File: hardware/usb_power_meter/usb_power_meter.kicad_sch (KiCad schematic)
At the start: 21 parts, among them U1 nRF52833-QDxx, X1 32.768kHz crystal, X2 32Mhz crystal

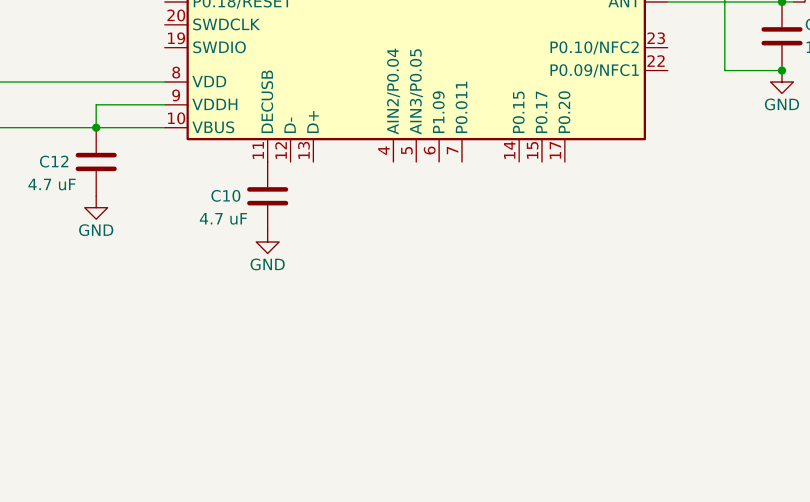
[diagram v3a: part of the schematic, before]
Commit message: Add INA226
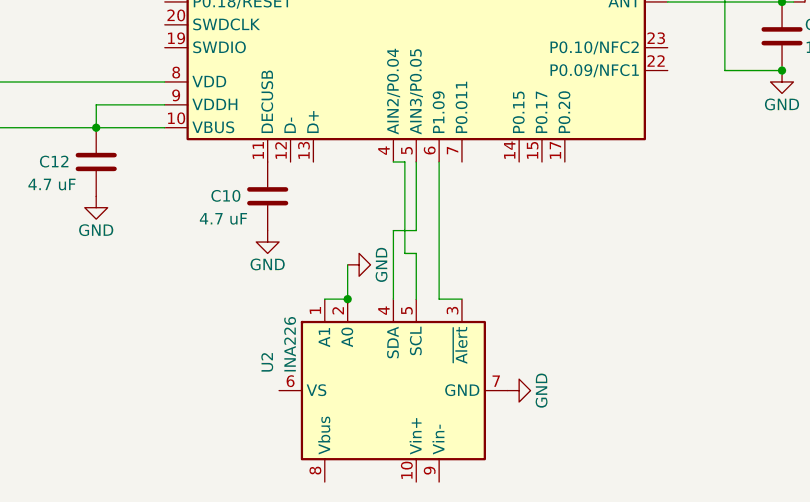
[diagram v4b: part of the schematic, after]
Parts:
- added U2: INA226, Package_SO:VSSOP-10_3x3mm_P0.5mm, symbol Ostranna:INA226
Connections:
- net GND: now also U2.1 (A1), U2.2 (A0), U2.7 (GND)
- net at U1.4 (AIN2/P0.04): now also U2.5 (SCL)
- net at U1.5 (AIN3/P0.05): now also U2.4 (SDA)
- net at U1.6 (P1.09): now also U2.3 (~{Alert})
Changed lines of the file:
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@@
   (junction (at 198.12 113.03) (diameter 0) (color 0 0 0 0)
+  )
+  (junction (at 138.43 146.05) (diameter 0) (color 0 0 0 0)
   )
   (junction (at 87.63 104.14) (diameter 0) (color 0 0 0 0)
@@
     (stroke (width 0) (type default))
   )
+  (wire (pts (xy 144.78 140.97) (xy 144.78 130.81))
+    (stroke (width 0) (type default))
+  )
+  (wire (pts (xy 143.51 138.43) (xy 146.05 138.43))
+    (stroke (width 0) (type default))
+  )
   (wire (pts (xy 83.82 111.76) (xy 87.63 111.76))
     (stroke (width 0) (type default))
@@
     (stroke (width 0) (type default))
   )
+  (wire (pts (xy 146.05 146.05) (xy 146.05 140.97))
+    (stroke (width 0) (type default))
+  )
   (wire (pts (xy 148.59 62.23) (xy 152.4 62.23))
     (stroke (width 0) (type default))
@@
     (stroke (width 0) (type default))
   )
+  (wire (pts (xy 146.05 140.97) (xy 144.78 140.97))
+    (stroke (width 0) (type default))
+  )
   (wire (pts (xy 148.59 80.01) (xy 148.59 62.23))
     (stroke (width 0) (type default))
@@
     (stroke (width 0) (type default))
   )
+  (wire (pts (xy 148.59 146.05) (xy 148.59 130.81))
+    (stroke (width 0) (type default))
+  )
   (wire (pts (xy 120.65 90.17) (xy 115.57 90.17))
     (stroke (width 0) (type default))
@@
     (stroke (width 0) (type default))
   )
+  (wire (pts (xy 138.43 146.05) (xy 138.43 142.24))
+    (stroke (width 0) (type default))
+  )
   (wire (pts (xy 102.87 88.9) (xy 96.52 88.9))
     (stroke (width 0) (type default))
@@
     (stroke (width 0) (type default))
   )
+  (wire (pts (xy 146.05 138.43) (xy 146.05 130.81))
+    (stroke (width 0) (type default))
+  )
   (wire (pts (xy 133.35 62.23) (xy 135.89 62.23))
     (stroke (width 0) (type default))
@@
     (stroke (width 0) (type default))
   )
+  (wire (pts (xy 151.13 146.05) (xy 148.59 146.05))
+    (stroke (width 0) (type default))
+  )
+  (wire (pts (xy 144.78 130.81) (xy 143.51 130.81))
+    (stroke (width 0) (type default))
+  )
   (wire (pts (xy 67.31 121.92) (xy 118.11 121.92))
     (stroke (width 0) (type default))
@@
     (stroke (width 0) (type default))
   )
+  (wire (pts (xy 135.89 146.05) (xy 138.43 146.05))
+    (stroke (width 0) (type default))
+  )
   (wire (pts (xy 118.11 106.68) (xy 102.87 106.68))
     (stroke (width 0) (type default))
   )
   (wire (pts (xy 134.62 71.12) (xy 133.35 71.12))
+    (stroke (width 0) (type default))
+  )
+  (wire (pts (xy 143.51 146.05) (xy 143.51 138.43))
     (stroke (width 0) (type default))
   )
@@
     )
   )
+  (symbol (lib_id "Ostranna:INA226") (at 143.51 156.21 90) (unit 1)
+    (in_bom yes) (on_board yes) (dnp no) (fields_autoplaced)
+    (property "Reference" "U2" (at 129.54 154.2541 0)
+      (effects (font (size 1.27 1.27)) (justify left))
+    )
+    (property "Value" "INA226" (at 132.08 154.2541 0)
+      (effects (font (size 1.27 1.27)) (justify left))
+    )
+    (property "Footprint" "Package_SO:VSSOP-10_3x3mm_P0.5mm" (at 154.94 135.89 0)
+      (effects (font (size 1.27 1.27)) hide)
+    )
+    (property "Datasheet" "http://www.ti.com/lit/ds/symlink/ina226.pdf" (at 146.05 147.32 0)
+      (effects (font (size 1.27 1.27)) hide)
+    )
+    (property "LCSC" "C49851" (at 143.51 156.21 0)
+      (effects (font (size 1.27 1.27)) hide)
+    )
+    (pin "1")
+    (pin "10")
+    (pin "2")
+    (pin "3")
+    (pin "4")
+    (pin "5")
+    (pin "6")
+    (pin "7")
+    (pin "8")
+    (pin "9")
+    (instances
+      (project "usb_power_meter"
+        (path "/991df1c7-1ea4-4c32-892f-6236282859f6"
+          (reference "U2") (unit 1)
+        )
+      )
+    )
+  )
   (symbol (lib_id "power:GND") (at 86.36 97.79 0) (unit 1)
     (in_bom yes) (on_board yes) (dnp no)
@@
         (path "/991df1c7-1ea4-4c32-892f-6236282859f6"
           (reference "#PWR04") (unit 1)
+        )
+      )
+    )
+  )
+  (symbol (lib_id "power:GND") (at 156.21 156.21 90) (unit 1)
+    (in_bom yes) (on_board yes) (dnp no)
+    (property "Reference" "#PWR020" (at 162.56 156.21 0)
+      (effects (font (size 1.27 1.27)) hide)
+    )
+    (property "Value" "GND" (at 160.02 156.21 0)
+      (effects (font (size 1.27 1.27)))
+    )
+    (property "Footprint" "" (at 156.21 156.21 0)
+      (effects (font (size 1.27 1.27)) hide)
+    )
+    (property "Datasheet" "" (at 156.21 156.21 0)
+      (effects (font (size 1.27 1.27)) hide)
+    )
+    (pin "1")
+    (instances
+      (project "usb_power_meter"
+        (path "/991df1c7-1ea4-4c32-892f-6236282859f6"
+          (reference "#PWR020") (unit 1)
         )
       )
@@
         )
       )
+    )
+  )
+  (symbol (lib_id "power:GND") (at 138.43 142.24 90) (unit 1)
+    (in_bom yes) (on_board yes) (dnp no)
+    (property "Reference" "#PWR021" (at 144.78 142.24 0)
+      (effects (font (size 1.27 1.27)) hide)
+    )
+    (property "Value" "GND" (at 142.24 142.24 0)
+      (effects (font (size 1.27 1.27)))
+    )
+    (property "Footprint" "" (at 138.43 142.24 0)
+      (effects (font (size 1.27 1.27)) hide)
+    )
+    (property "Datasheet" "" (at 138.43 142.24 0)
+      (effects (font (size 1.27 1.27)) hide)
+    )
+    (pin "1")
+    (instances
+      (project "usb_power_meter"
+        (path "/991df1c7-1ea4-4c32-892f-6236282859f6"
+          (reference "#PWR021") (unit 1)
+        )
+      )

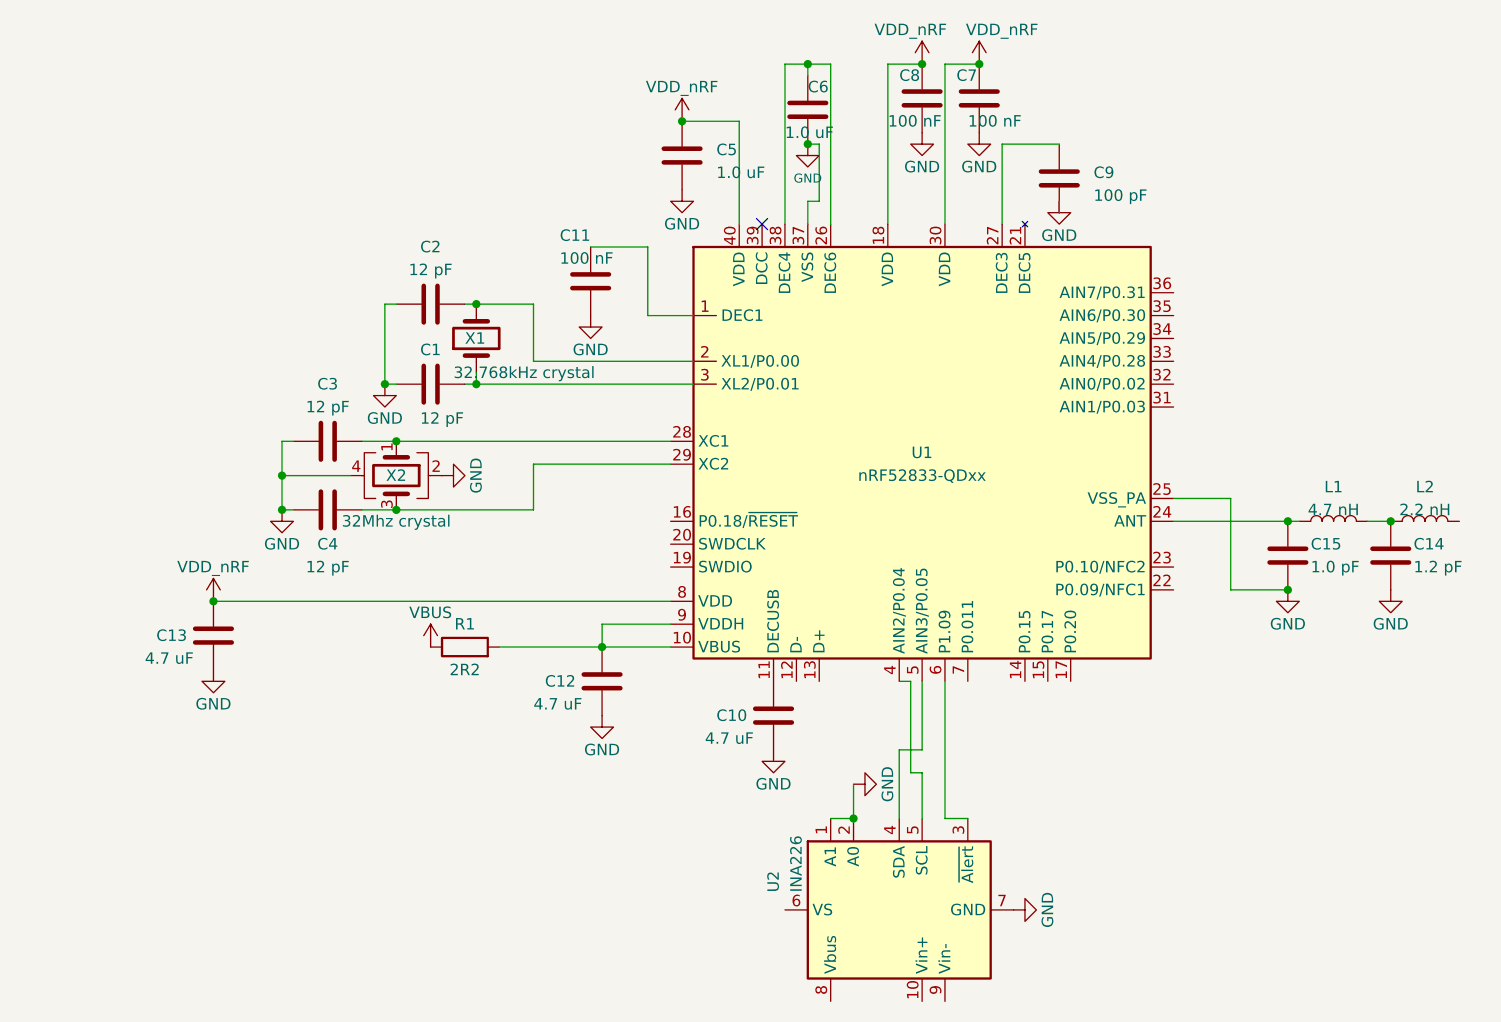
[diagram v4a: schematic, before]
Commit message: Draft component positions
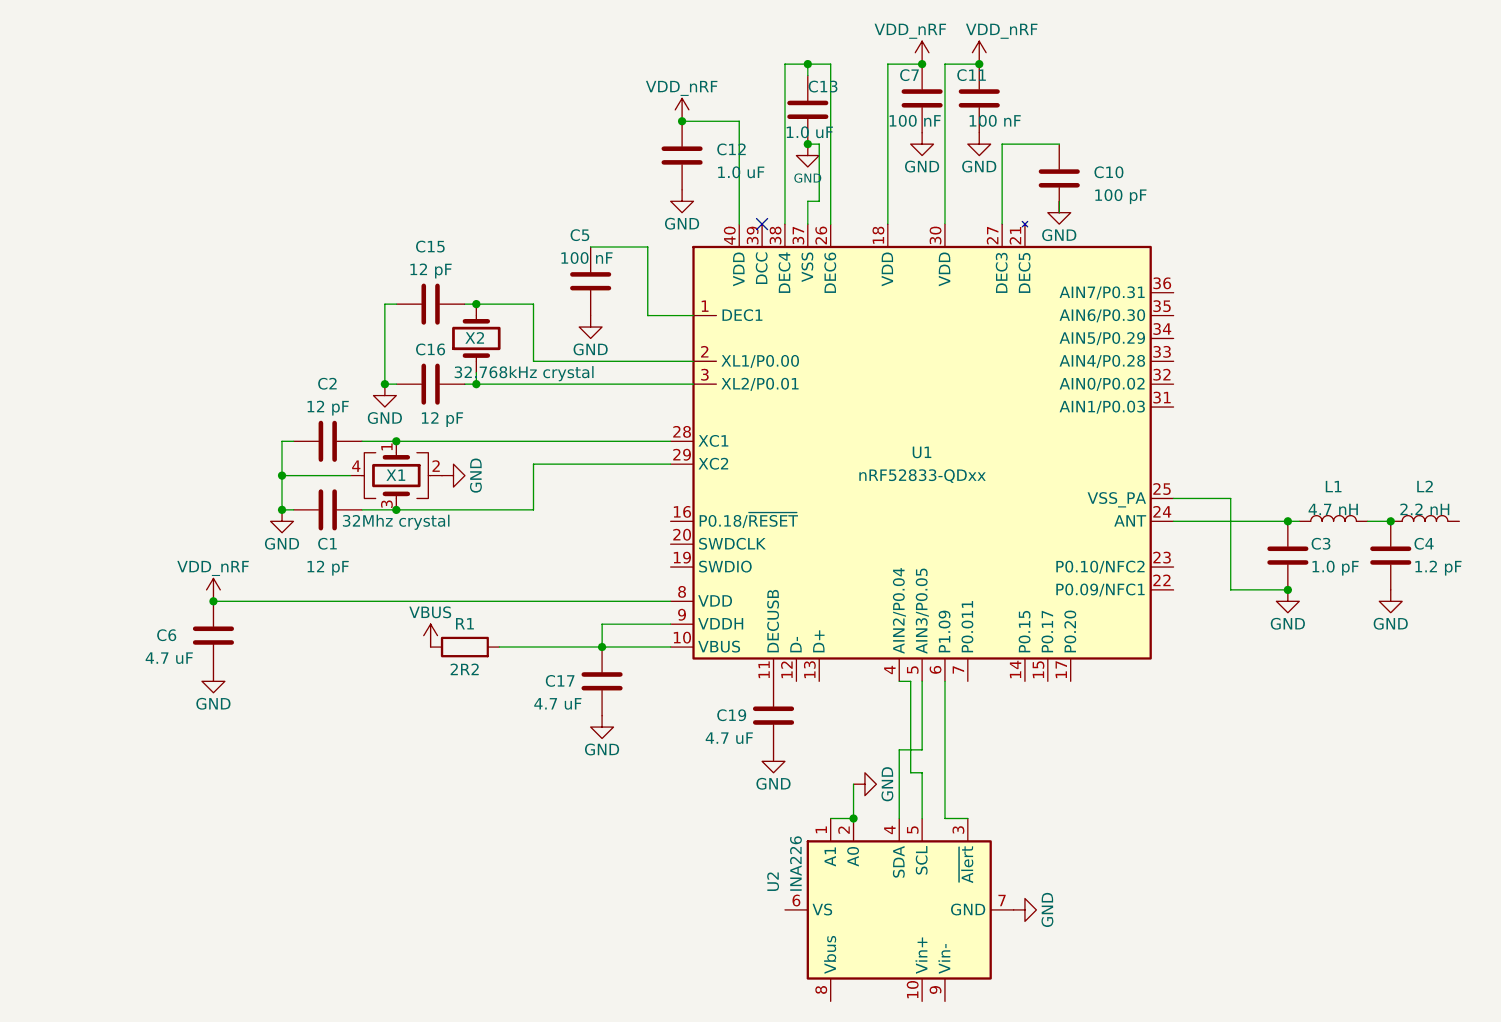
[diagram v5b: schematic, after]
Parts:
- renumbered C4 to C1, C9 to C10, C7 to C11, C5 to C12, C6 to C13, C2 to C15, C1 to C16, C12 to C17, C10 to C19, C3 to C2, C15 to C3, C14 to C4, C11 to C5, C13 to C6, C8 to C7, X2 to X1, X1 to X2
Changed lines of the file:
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@@
   (symbol (lib_id "Ostranna:12 pF") (at 80.01 104.14 90) (unit 1)
     (in_bom yes) (on_board yes) (dnp no)
-    (property "Reference" "C3" (at 80.01 97.79 90)
+    (property "Reference" "C2" (at 80.01 97.79 90)
       (effects (font (size 1.27 1.27)))
     )
@@
       (project "usb_power_meter"
         (path "/991df1c7-1ea4-4c32-892f-6236282859f6"
-          (reference "C3") (unit 1)
+          (reference "C2") (unit 1)
         )
       )
@@
   (symbol (lib_id "Ostranna:12 pF") (at 91.44 88.9 90) (unit 1)
     (in_bom yes) (on_board yes) (dnp no) (fields_autoplaced)
-    (property "Reference" "C2" (at 91.44 82.55 90)
+    (property "Reference" "C15" (at 91.44 82.55 90)
       (effects (font (size 1.27 1.27)))
     )
@@
       (project "usb_power_meter"
         (path "/991df1c7-1ea4-4c32-892f-6236282859f6"
-          (reference "C2") (unit 1)
+          (reference "C15") (unit 1)
         )
       )
@@
   (symbol (lib_id "Ostranna:4.7 uF") (at 129.54 134.62 0) (unit 1)
     (in_bom yes) (on_board yes) (dnp no)
-    (property "Reference" "C10" (at 123.19 134.62 0)
+    (property "Reference" "C19" (at 123.19 134.62 0)
       (effects (font (size 1.27 1.27)) (justify left))
     )
@@
       (project "usb_power_meter"
         (path "/991df1c7-1ea4-4c32-892f-6236282859f6"
-          (reference "C10") (unit 1)
+          (reference "C19") (unit 1)
         )
       )
@@
   (symbol (lib_id "Ostranna:4.7 uF") (at 67.31 125.73 0) (unit 1)
     (in_bom yes) (on_board yes) (dnp no)
-    (property "Reference" "C13" (at 60.96 125.73 0)
+    (property "Reference" "C6" (at 60.96 125.73 0)
       (effects (font (size 1.27 1.27)) (justify left))
     )
@@
       (project "usb_power_meter"
         (path "/991df1c7-1ea4-4c32-892f-6236282859f6"
-          (reference "C13") (unit 1)
+          (reference "C6") (unit 1)
         )
       )
@@
   (symbol (lib_id "Ostranna:1.0 uF") (at 119.38 72.39 0) (unit 1)
     (in_bom yes) (on_board yes) (dnp no) (fields_autoplaced)
-    (property "Reference" "C5" (at 123.19 71.755 0)
+    (property "Reference" "C12" (at 123.19 71.755 0)
       (effects (font (size 1.27 1.27)) (justify left))
     )
@@
       (project "usb_power_meter"
         (path "/991df1c7-1ea4-4c32-892f-6236282859f6"
-          (reference "C5") (unit 1)
+          (reference "C12") (unit 1)
         )
       )
@@
   (symbol (lib_id "Ostranna:4.7 uF") (at 110.49 130.81 0) (unit 1)
     (in_bom yes) (on_board yes) (dnp no)
-    (property "Reference" "C12" (at 104.14 130.81 0)
+    (property "Reference" "C17" (at 104.14 130.81 0)
       (effects (font (size 1.27 1.27)) (justify left))
     )
@@
       (project "usb_power_meter"
         (path "/991df1c7-1ea4-4c32-892f-6236282859f6"
-          (reference "C12") (unit 1)
+          (reference "C17") (unit 1)
         )
       )
@@
   (symbol (lib_id "Ostranna:100 pF") (at 161.29 74.93 0) (unit 1)
     (in_bom yes) (on_board yes) (dnp no) (fields_autoplaced)
-    (property "Reference" "C9" (at 165.1 74.295 0)
+    (property "Reference" "C10" (at 165.1 74.295 0)
       (effects (font (size 1.27 1.27)) (justify left))
     )
@@
       (project "usb_power_meter"
         (path "/991df1c7-1ea4-4c32-892f-6236282859f6"
-          (reference "C9") (unit 1)
+          (reference "C10") (unit 1)
         )
       )
@@
   (symbol (lib_id "Ostranna:1.0 uF") (at 133.35 67.31 0) (unit 1)
     (in_bom yes) (on_board yes) (dnp no)
-    (property "Reference" "C6" (at 133.35 64.77 0)
+    (property "Reference" "C13" (at 133.35 64.77 0)
       (effects (font (size 1.27 1.27)) (justify left))
     )
@@
       (project "usb_power_meter"
         (path "/991df1c7-1ea4-4c32-892f-6236282859f6"
-          (reference "C6") (unit 1)
+          (reference "C13") (unit 1)
         )
       )
@@
   (symbol (lib_id "Ostranna:100 nF") (at 146.05 66.04 0) (unit 1)
     (in_bom yes) (on_board yes) (dnp no)
-    (property "Reference" "C8" (at 143.51 63.5 0)
+    (property "Reference" "C7" (at 143.51 63.5 0)
       (effects (font (size 1.27 1.27)) (justify left))
     )
@@
       (project "usb_power_meter"
         (path "/991df1c7-1ea4-4c32-892f-6236282859f6"
-          (reference "C8") (unit 1)
+          (reference "C7") (unit 1)
         )
       )
@@
   (symbol (lib_id "Ostranna:12 pF") (at 80.01 111.76 90) (unit 1)
     (in_bom yes) (on_board yes) (dnp no)
-    (property "Reference" "C4" (at 80.01 115.57 90)
+    (property "Reference" "C1" (at 80.01 115.57 90)
       (effects (font (size 1.27 1.27)))
     )
@@
       (project "usb_power_meter"
         (path "/991df1c7-1ea4-4c32-892f-6236282859f6"
-          (reference "C4") (unit 1)
+          (reference "C1") (unit 1)
         )
       )
@@
   (symbol (lib_id "Ostranna:12 pF") (at 91.44 97.79 90) (unit 1)
     (in_bom yes) (on_board yes) (dnp no)
-    (property "Reference" "C1" (at 91.44 93.98 90)
+    (property "Reference" "C16" (at 91.44 93.98 90)
       (effects (font (size 1.27 1.27)))
     )
@@
       (project "usb_power_meter"
         (path "/991df1c7-1ea4-4c32-892f-6236282859f6"
-          (reference "C1") (unit 1)
+          (reference "C16") (unit 1)
         )
       )
@@
   (symbol (lib_id "Ostranna:1.2 pF") (at 198.12 116.84 0) (unit 1)
     (in_bom yes) (on_board yes) (dnp no)
-    (property "Reference" "C14" (at 200.66 115.57 0)
+    (property "Reference" "C4" (at 200.66 115.57 0)
       (effects (font (size 1.27 1.27)) (justify left))
     )
@@
       (project "usb_power_meter"
         (path "/991df1c7-1ea4-4c32-892f-6236282859f6"
-          (reference "C14") (unit 1)
+          (reference "C4") (unit 1)
         )
       )
@@
   (symbol (lib_id "Ostranna:100 nF") (at 152.4 66.04 0) (unit 1)
     (in_bom yes) (on_board yes) (dnp no)
-    (property "Reference" "C7" (at 149.86 63.5 0)
+    (property "Reference" "C11" (at 149.86 63.5 0)
       (effects (font (size 1.27 1.27)) (justify left))
     )
@@
       (project "usb_power_meter"
         (path "/991df1c7-1ea4-4c32-892f-6236282859f6"
-          (reference "C7") (unit 1)
+          (reference "C11") (unit 1)
         )
       )
@@
   (symbol (lib_id "Ostranna:100 nF") (at 109.22 86.36 180) (unit 1)
     (in_bom yes) (on_board yes) (dnp no)
-    (property "Reference" "C11" (at 109.22 81.28 0)
+    (property "Reference" "C5" (at 109.22 81.28 0)
       (effects (font (size 1.27 1.27)) (justify left))
     )
@@
       (project "usb_power_meter"
         (path "/991df1c7-1ea4-4c32-892f-6236282859f6"
-          (reference "C11") (unit 1)
+          (reference "C5") (unit 1)
         )
       )
@@
   (symbol (lib_id "Ostranna:1.0 pF") (at 186.69 116.84 0) (unit 1)
     (in_bom yes) (on_board yes) (dnp no)
-    (property "Reference" "C15" (at 189.23 115.57 0)
+    (property "Reference" "C3" (at 189.23 115.57 0)
       (effects (font (size 1.27 1.27)) (justify left))
     )
@@
       (project "usb_power_meter"
         (path "/991df1c7-1ea4-4c32-892f-6236282859f6"
-          (reference "C15") (unit 1)
+          (reference "C3") (unit 1)
         )
       )
@@
   (symbol (lib_id "Ostranna:32Mhz crystal") (at 87.63 107.95 270) (unit 1)
     (in_bom yes) (on_board yes) (dnp no)
-    (property "Reference" "X2" (at 87.63 107.95 90)
+    (property "Reference" "X1" (at 87.63 107.95 90)
       (effects (font (size 1.27 1.27)))
     )
@@
       (project "usb_power_meter"
         (path "/991df1c7-1ea4-4c32-892f-6236282859f6"
-          (reference "X2") (unit 1)
+          (reference "X1") (unit 1)
         )
       )
@@
   (symbol (lib_id "Ostranna:32.768kHz crystal") (at 96.52 92.71 90) (unit 1)
     (in_bom yes) (on_board yes) (dnp no)
-    (property "Reference" "X1" (at 95.25 92.71 90)
+    (property "Reference" "X2" (at 95.25 92.71 90)
       (effects (font (size 1.27 1.27)) (justify right))
     )
@@
       (project "usb_power_meter"
         (path "/991df1c7-1ea4-4c32-892f-6236282859f6"
-          (reference "X1") (unit 1)
-        )
-      )
+          (reference "X2") (unit 1)
+        )
+      )
